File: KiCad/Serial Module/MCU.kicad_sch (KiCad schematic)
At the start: 33 parts, among them J2 Conn_ARM_SWD_TagConnect_TC2030, U1 STM32F411RETx, U7 74LVC1G126, U8 74LVC1G126, X1 25Mhz

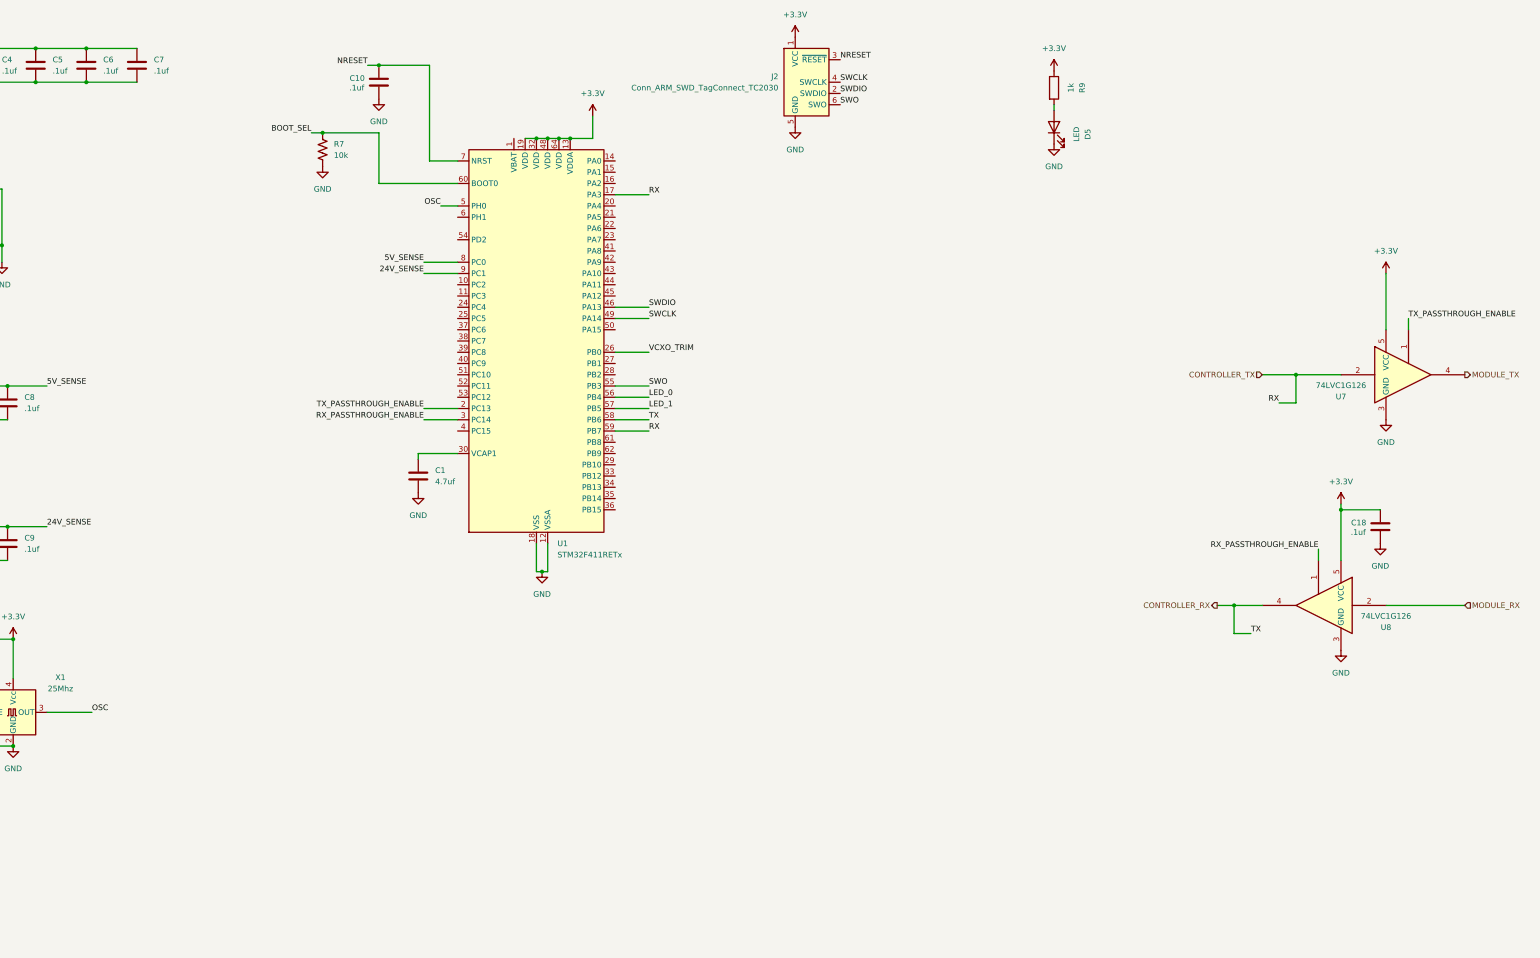
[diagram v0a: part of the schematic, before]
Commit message: update serial module and backplane hw
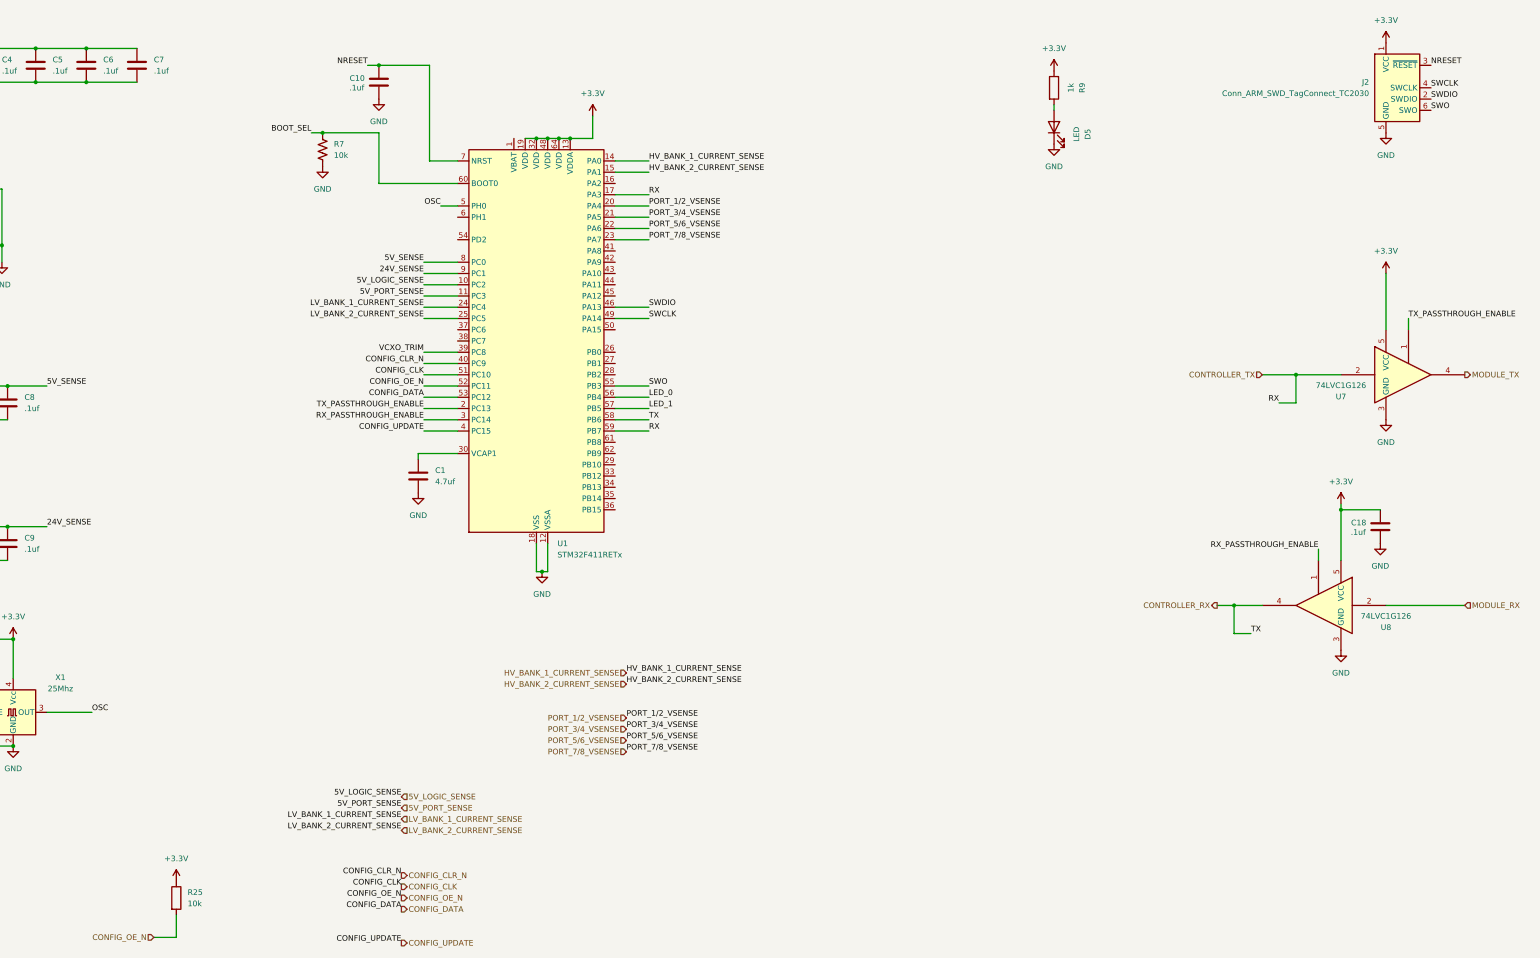
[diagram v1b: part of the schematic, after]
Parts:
- added R25: 10k, Resistor_SMD:R_0603_1608Metric, symbol Device:R
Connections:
- net +3.3V: now also R25.1
- net VCXO_TRIM: now also U1.39 (PC8); no longer U1.26 (PB0)
- net 5V_LOGIC_SENSE: now reaches U1.10 (PC2)
- net 5V_PORT_SENSE: now reaches U1.11 (PC3)
- net HV_BANK_1_CURRENT_SENSE: now reaches U1.14 (PA0)
- net HV_BANK_2_CURRENT_SENSE: now reaches U1.15 (PA1)
- net PORT_1/2_VSENSE: now reaches U1.20 (PA4)
- net PORT_3/4_VSENSE: now reaches U1.21 (PA5)
- net PORT_5/6_VSENSE: now reaches U1.22 (PA6)
- net PORT_7/8_VSENSE: now reaches U1.23 (PA7)
- net LV_BANK_1_CURRENT_SENSE: now reaches U1.24 (PC4)
- net LV_BANK_2_CURRENT_SENSE: now reaches U1.25 (PC5)
- net CONFIG_UPDATE: now reaches U1.4 (PC15)
- net CONFIG_CLR_N: now reaches U1.40 (PC9)
- net CONFIG_CLK: now reaches U1.51 (PC10)
- net CONFIG_OE_N: now reaches U1.52 (PC11)
- net CONFIG_OE_N: now also R25.2
- net CONFIG_DATA: now reaches U1.53 (PC12)
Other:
- moved on the sheet: J2

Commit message: add current limit and sense parts, add possible endat solution
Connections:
- net FAULT_N_HV_BANK_1: now reaches U1.29 (PB10)
- net FAULT_N_HV_BANK_2: now reaches U1.33 (PB12)
- net FAULT_N_LV_BANK_1: now reaches U1.61 (PB8)
- net FAULT_N_LV_BANK_2: now reaches U1.62 (PB9)
